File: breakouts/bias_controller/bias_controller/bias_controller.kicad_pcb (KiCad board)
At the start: 2 copper layers, 196 parts, among them J201 Conn_01x03_Pin, J301 USB_C_Receptacle_USB2.0, Q301 AO3400A, Q302 AO4407, U201 RP2040, U202 W25Q128JVSIQ, U203 TXB0104RGY, U204 TXB0104RGY, U205 TXB0104RGY, U206 M24C02-WMN, U301 LDR6321, U401 DAC5311IDCKR, U402 DAC5311IDCKR, U403 DAC5311IDCKR, U404 DAC5311IDCKR, U405 LM324DT, U406 LM324DT, U407 LM324DT, U601 LM2776, U602 TPS63070RNMT, U603 LT3094xMSE, U604 ADM7172, U605 ADM7172, U606 ADM7172, U701 TPS22917DBV, U702 TPS22917DBV, U703 INA199B1DCKR

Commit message: schematic and footprint assignment cleanup
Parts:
- removed C704: 100 nF, Capacitor_SMD:C_0402_1005Metric
- removed the U406 at (72.3, 83.2)
- removed U407: LM324DT, Package_SO:SO-14_3.9x8.65mm_P1.27mm
- added C504: 1 uF, Capacitor_SMD:C_0402_1005Metric, F.Cu at (106.2, 93.8)
- added C505: 1 uF, Capacitor_SMD:C_0402_1005Metric, F.Cu at (106.2, 95.8)
- added D301: ESD9B5VL, jtk_rf_footprints:DFN1006-2, F.Cu at (131.7, 99.7)
- added D302: ESD9B5VL, jtk_rf_footprints:DFN1006-2, F.Cu at (131.7, 101.6)
- added J801: Conn_02x20_Odd_Even, snapeda:TE_5177986-1, F.Cu at (116.6, 103.0)
- added R213: 0, Resistor_SMD:R_0402_1005Metric, F.Cu at (130.4, 90.2)
- added SW201: SW_Push, Button_Switch_SMD:SW_Push_1P1T_XKB_TS-1187A, F.Cu at (129.1, 74.3)
- added SW202: SW_Push, Button_Switch_SMD:SW_Push_1P1T_XKB_TS-1187A, F.Cu at (128.0, 85.9)
- added U501: LM324DT, Package_SO:SO-14_3.9x8.65mm_P1.27mm, F.Cu at (109.0, 87.7)
- added U503: LM324DT, Package_SO:SO-14_3.9x8.65mm_P1.27mm, F.Cu at (117.5, 87.7)
- added Y202: XL2EL89COI-111YLC-12M, Crystal:Crystal_SMD_3225-4Pin_3.2x2.5mm, F.Cu at (126.3, 91.5)
- C201, C202: value 27 pF -> 20 pF
- R603: value 10k -> 470k
- R604: value 10k -> 150k
- R605: value 10k -> 360k
- R703: value R_Small -> 0.05
- R704: value R_Small -> 0
- renumbered U405 to U406
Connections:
- C202 pad 2: Net-(U201-XOUT) -> Net-(C202-Pad2)
- C501 pad 1: Net-(U405D-+) -> Net-(U501A-+)
- R415 pad 2: Net-(U406A-+) -> Net-(U406B-+)
- R416 pad 2: Net-(U407A-+) -> Net-(U406C-+)
- R422 pad 2: Net-(U406A--) (its old number) -> Net-(U406B--)
- R423 pad 2: Net-(U407A--) -> Net-(U406C--)
- R424 pad 1: Net-(U406A--) (its old number) -> Net-(U406B--)
- R425 pad 1: Net-(U407A--) -> Net-(U406C--)
- R501 pad 2: Net-(U405C-+) -> Net-(U501C-+)
- R502 pad 2: Net-(U405C-+) -> Net-(U501C-+)
- R503 pad 2: Net-(U405B-+) -> Net-(U501B-+)
- R504 pad 2: Net-(U405B-+) -> Net-(U501B-+)
- R505 pad 1: Net-(U405D-+) -> Net-(U501A-+)
- R506 pad 2: Net-(U405D-+) -> Net-(U501A-+)
- R507 pad 2: Net-(U405C--) -> Net-(U501C--)
- R508 pad 2: Net-(U405B--) -> Net-(U501B--)
- R509 pad 1: Net-(U405C--) -> Net-(U501C--)
- R510 pad 1: Net-(U405B--) -> Net-(U501B--)
- R704 pad 2: +3.3VP -> GND
- U406 pad 10: Net-(U405C-+) -> Net-(U406C-+)
- U406 pad 12: Net-(U405D-+) -> GND
- U406 pad 13: /telemetry/Vref_telem -> Net-(U406D--)
- U406 pad 14: /telemetry/Vref_telem -> Net-(U406D--)
- U406 pad 5: Net-(U405B-+) -> Net-(U406B-+)
- U406 pad 6: Net-(U405B--) -> Net-(U406B--)
- U406 pad 7: Net-(R510-Pad2) -> Net-(R424-Pad2)
- U406 pad 8: Net-(R509-Pad2) -> Net-(R425-Pad2)
- U406 pad 9: Net-(U405C--) -> Net-(U406C--)
- U602 pad 12_13: (no net) -> Vusb
- U602 pad 7_8: (no net) -> VPP

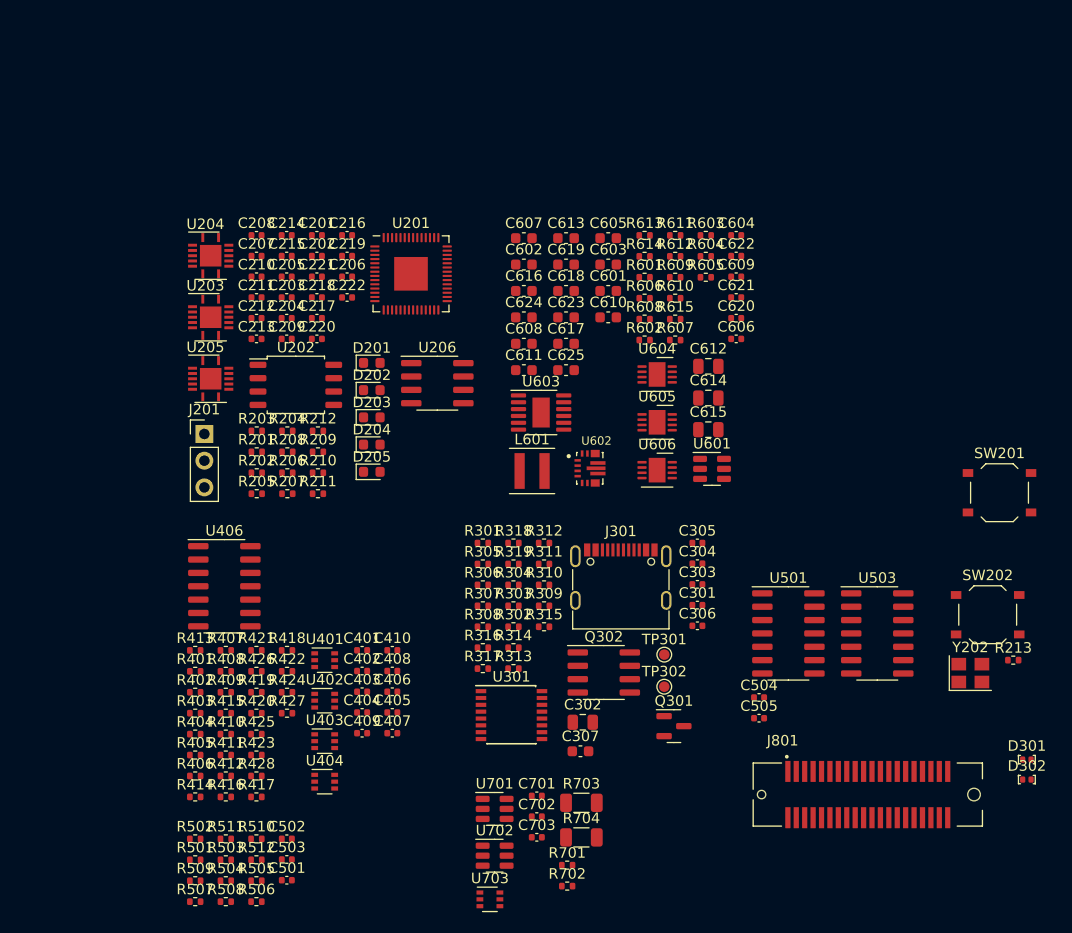
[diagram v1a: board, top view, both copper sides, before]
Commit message: more cleanup and part number assignsments on bias controller
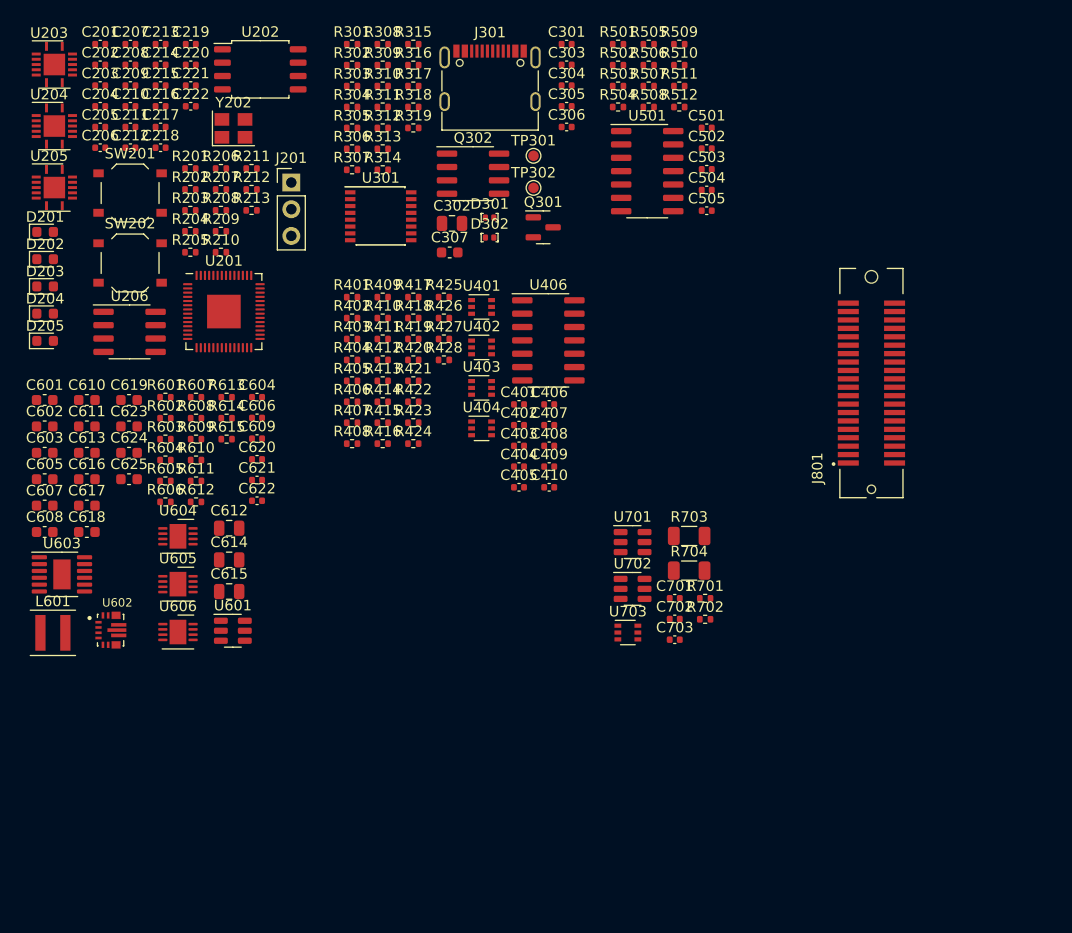
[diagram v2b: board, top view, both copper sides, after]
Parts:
- removed U503: LM324DT, Package_SO:SO-14_3.9x8.65mm_P1.27mm
- moved R509 91.9 mm to (98.6, 31.7)
- moved R507 88.7 mm to (95.7, 35.7)
- moved SW202 88.1 mm to (46.4, 52.5)
- moved R505 87.9 mm to (95.7, 31.7)
- moved R506 87.9 mm to (95.7, 33.7)
- moved SW201 87.4 mm to (46.4, 45.8)
- moved R501 87.4 mm to (92.8, 31.7)
- moved Y202 87.1 mm to (56.2, 39.7)
- moved R508 85.6 mm to (95.7, 37.6)
- moved R213 84.1 mm to (58.0, 47.5)
- moved R502 83.8 mm to (92.8, 33.7)
- moved R510 83.8 mm to (98.6, 33.7)
- moved R511 83.6 mm to (98.6, 35.7)
- moved R503 82.5 mm to (92.8, 35.7)
- moved R504 82.5 mm to (92.8, 37.6)
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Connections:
- U501 pad 11: (no net) -> -6V
- U501 pad 4: (no net) -> VPP
